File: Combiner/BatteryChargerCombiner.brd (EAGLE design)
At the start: 190.5 x 42 mm, 183 parts, among them Q1 DMN6040SSD-13, Q10 4.3A/20V/54mΩ, Q11 4.3A/20V/54mΩ, Q2 DMN6040SSD-13, Q3 DMN6040SSD-13, Q4 DMN6040SSD-13, Q5 DMP4047SSD-13, Q6 220mA/50V/3.5Ω, Q7 220mA/50V/3.5Ω, Q8 4.3A/20V/54mΩ, Q9 4.3A/20V/54mΩ, U1 BQ24650, U10 TS7211, U11 MIC5219 3.3V, U12 MKR1000-SMD, U13 STWD100, U14 74AUC1G06DBV, U15 74AUC1G06DBV, U16 74AUC1G06DBV, U17 LMV358, U2 BQ28Z610, U3 BQ28Z610, U4 BQ24650, U5 TCA9543A, U6 WE-78, U7 WE-78, U8 74AHC1G07DBV, U9 74AUC1G06DBV

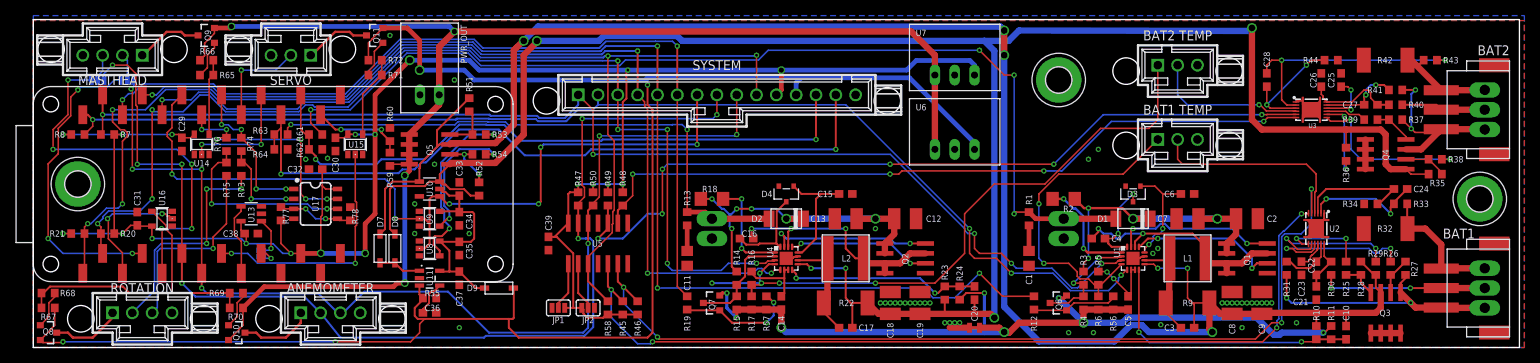
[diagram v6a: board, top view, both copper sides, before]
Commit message: Shrunk board width to 1600 mil, so it will fit inside a 1.5 in PVC pipe
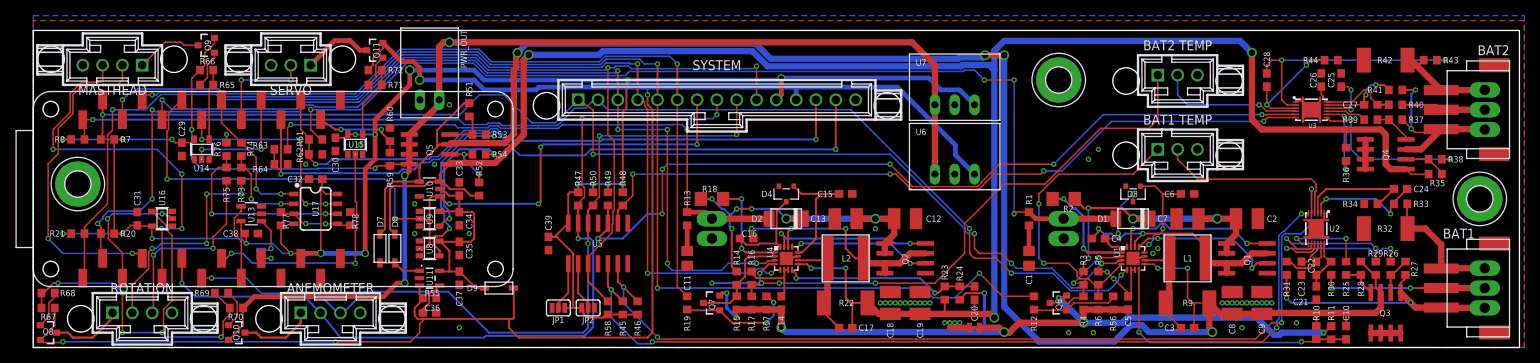
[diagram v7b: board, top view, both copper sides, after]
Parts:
- removed JP3, JP4: JUMPER-SMT_3_NO_SILK, SparkFun-Jumpers:SMT-JUMPER_3_NO_SILK
- moved U7 3.81 mm to (118.1, 31.1)
- moved U6 3.17 mm to (118.1, 22.2)
- moved Q11 1.91 mm to (43.8, 38.1)
- moved R63 1.91 mm to (31.8, 25.4)
- moved R69 1.91 mm to (24.1, 6.99)
- moved R64 1.90 mm to (31.8, 23.5)
- moved BAT1_TS 1.27 mm to (146.7, 25.4)
- moved BAT2_TS 1.27 mm to (146.7, 34.9)
- moved MASTHEAD 1.27 mm to (10.2, 36.2)
- moved Q9 1.27 mm to (22.2, 38.7)
- moved TAIL 1.27 mm to (33.0, 36.2)
- moved C32 1.27 mm to (36.2, 21.6)
- moved R65 1.27 mm to (22.2, 33.7)
- moved R66 1.27 mm to (22.2, 35.6)
- moved R71 1.27 mm to (43.8, 33.7)
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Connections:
- removed net N$14: JP3.2, MASTHEAD.P$2
- removed net N$47: JP4.2, MASTHEAD.P$3
- net DIM: now also MASTHEAD.P$3; no longer JP4.3
- net NEOPIXEL: now also MASTHEAD.P$2; no longer JP3.3
- net SCL: no longer JP3.1
- net SDA: no longer JP4.1
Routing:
- net SDA: track 143.8 -> 107.9 mm, vias 7 -> 4
- net SCL: track 138.1 -> 102.3 mm, vias 7 -> 4
- net N$69: track 40.2 -> 55.6 mm, vias 0 -> 5
- net VSELECT: track 175.3 -> 183.4 mm, vias 4 -> 5
- net +3V3: track 261.4 -> 256.3 mm
- net VBAT2: track 254.3 -> 249.4 mm
- net BAT2_STAT2: track 144.7 -> 140.2 mm, vias 6 -> 4
- net N$47: track 3.44 -> 0.00 mm
- net N$14: track 3.44 -> 0.00 mm
- net VBAT1: track 227.3 -> 224.0 mm
- net +5V: track 223.5 -> 220.4 mm
- net !I2C_RST!: track 122.6 -> 120.1 mm
- net SCL2: track 104.8 -> 107.2 mm
- net !BAT2_CE!: track 111.0 -> 108.5 mm
- net NEOPIXEL: track 39.5 -> 41.9 mm, vias 3 -> 2
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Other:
- board size 190.5 x 42 mm -> 190.5 x 40.6 mm

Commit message: Now with idiot lights; still need to fix silkscreen around lights
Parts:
- added 3V3_PWR: GRN, adafruit:CHIP-LED0603
- added 5V_PWR: BLU, adafruit:CHIP-LED0603
- added BAT1_PWR, BAT2_PWR, PANEL1_PWR, PANEL2_PWR: (no value), adafruit:CHIP-LED0603
- added BAT1_STAT1, BAT1_STAT2, BAT2_STAT1, BAT2_STAT2: RED, adafruit:CHIP-LED0603
- added R79, R80, R81, R82, R83, R84: 1K, resistor:R0603
- added R85, R86, R87, R88: 10K, resistor:R0603
- moved D4 8.03 mm to (104.1, 22.2), turned to 90 degrees
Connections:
- new net N$14: BAT1_STAT1.C, R79.1
- new net N$47: BAT1_STAT2.C, R80.1
- new net N$49: BAT2_STAT1.C, R81.1
- new net N$56: BAT2_STAT2.C, R82.1
- new net N$74: 3V3_PWR.C, R83.2
- new net N$77: 5V_PWR.C, R84.2
- new net N$81: BAT1_PWR.C, R85.2
- new net N$82: BAT2_PWR.C, R86.2
- new net N$83: PANEL1_PWR.C, R87.2
- new net N$84: PANEL2_PWR.C, R88.2
- net +3V3: now also 3V3_PWR.A, BAT1_STAT1.A, BAT1_STAT2.A, BAT2_STAT1.A, BAT2_STAT2.A
- net +5V: now also 5V_PWR.A
- net BAT1: now also BAT1_PWR.A
- net BAT1_STAT1: now also R79.2
- net BAT1_STAT2: now also R80.2
- net BAT2: now also BAT2_PWR.A
- net BAT2_STAT1: now also R81.2
- net BAT2_STAT2: now also R82.2
- net GND: now also R83.1, R84.1, R85.1, R86.1, R87.1, R88.1
- net PANEL1: now also PANEL1_PWR.A
- net PANEL2: now also PANEL2_PWR.A
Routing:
- net BAT1: track 33.3 -> 78.0 mm, vias 2 -> 6
- net PANEL1: track 129.3 -> 171.0 mm, vias 4 -> 7
- net BAT2: track 23.3 -> 52.4 mm, vias 2 -> 4
- net BAT2_STAT2: track 140.2 -> 158.0 mm, vias 4 -> 6
- net BAT1_STAT2: track 151.7 -> 168.0 mm, vias 4 -> 7
- net BAT2_STAT1: track 134.7 -> 148.3 mm, vias 8 -> 10
- net +3V3: track 256.3 -> 269.5 mm
- net PANEL2: track 76.5 -> 84.6 mm, vias 2 -> 3
- net N$17: track 11.6 -> 19.7 mm
- net +5V: track 220.4 -> 226.5 mm
- net BAT1_STAT1: track 155.4 -> 159.3 mm, vias 5 -> 6
- net N$84: track 0.00 -> 1.57 mm
- net N$83: track 0.00 -> 1.57 mm
- net N$77: track 0.00 -> 1.57 mm
- net N$74: track 0.00 -> 1.57 mm
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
